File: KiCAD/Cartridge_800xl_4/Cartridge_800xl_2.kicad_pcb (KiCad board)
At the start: 4 copper layers, 64 x 80.2 mm, 21 parts, among them SW1 Reset, U1 27C512, U2 74HC165, U3 74HC595, U4 GAL16V8, U5 TXS0108EPW, U6 mini_esp32

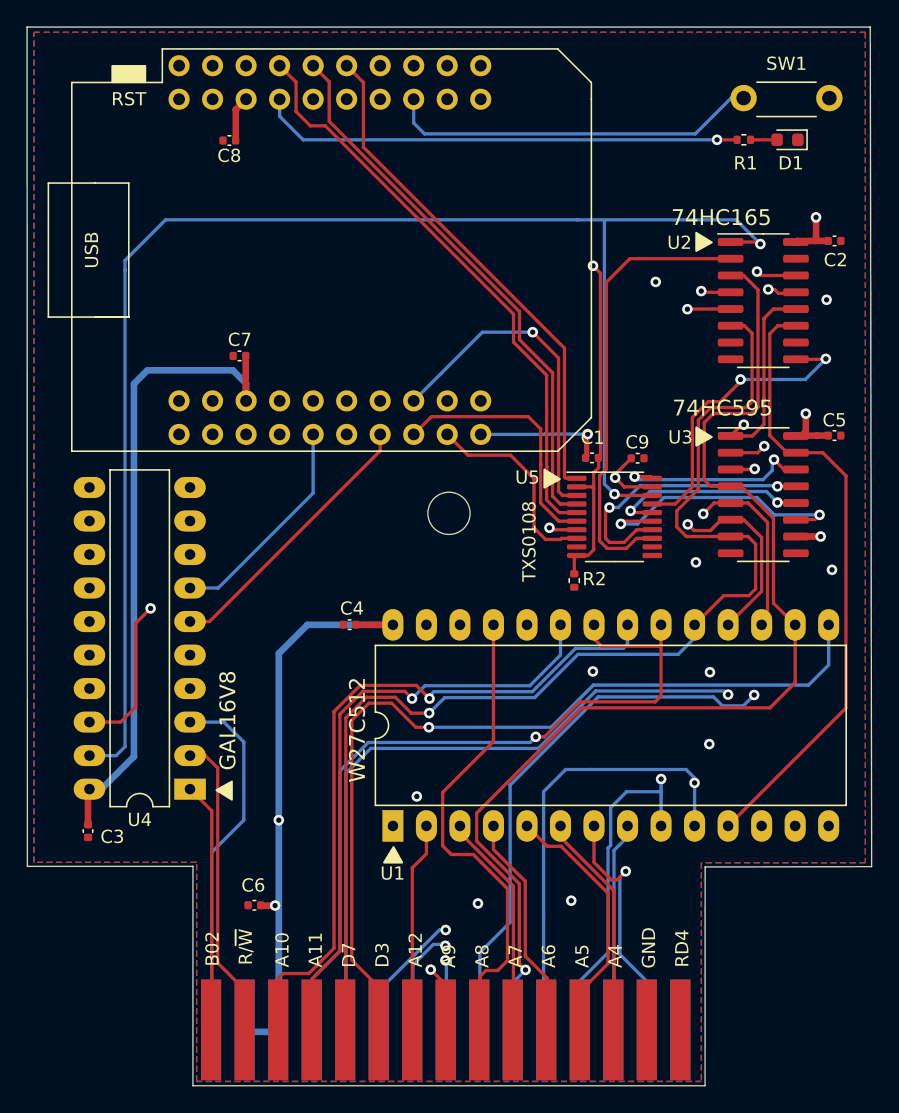
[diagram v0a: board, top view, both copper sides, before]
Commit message: version 3
No more sub version in file name
Fixed the userlist issue
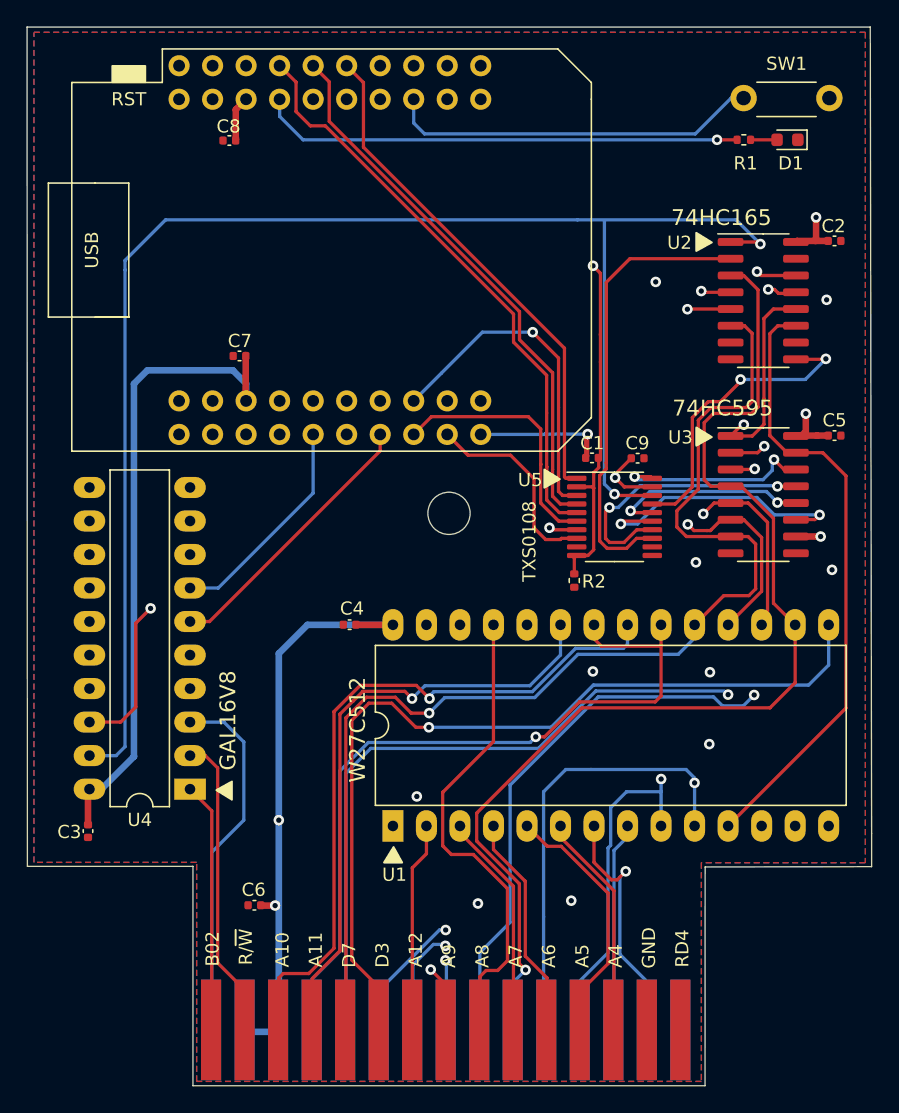
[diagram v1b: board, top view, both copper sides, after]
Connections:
- net IO1 renamed IO1H
- net IO2 renamed IO2H
- net iIO2 renamed IO2L
- U6 pad 25: iIO1 -> IO1L

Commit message: 3.78 release
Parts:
- moved C6 6.45 mm to (137.2, 120.3)
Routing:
- net +5V: track 201.9 -> 201.6 mm, vias 6 -> 5
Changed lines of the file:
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@@
   )
   (footprint "Capacitor_SMD:C_0402_1005Metric" (layer "F.Cu")
-    (at 136.900148 126.7125 180)
+    (at 137.2235 120.269 180)
     (descr "Capacitor SMD 0402 (1005 Metric), square (rectangular) end terminal, IPC_7351 nominal, (Body size source: IPC-SM-782 page 76, https://www.pcb-3d.com/wordpress/wp-content/uploads/ipc-sm-782a_amendment_1_and_2.pdf), generated with kicad-footprint-generator")
     (tags "capacitor")
@@
   (segment (start 136.240148 85.0125) (end 136.240148 86.6175) (width 0.5) (layer "F.Cu") (net 24))
   (segment (start 144.605148 105.461359) (end 144.595148 105.451359) (width 0.5) (layer "F.Cu") (net 24))
-  (segment (start 137.405148 126.7375) (end 137.380148 126.7125) (width 0.5) (layer "F.Cu") (net 24))
   (segment (start 136.240148 86.6175) (end 136.240148 88.4625) (width 0.5) (layer "F.Cu") (net 24))
   (segment (start 136.240148 88.4625) (end 136.270148 88.4925) (width 0.5) (layer "F.Cu") (net 24))
@@
   (segment (start 180.38048 76.37) (end 179.39798 76.37) (width 0.5) (layer "F.Cu") (net 24))
   (segment (start 179.46048 74.5825) (end 179.46048 76.3075) (width 0.5) (layer "F.Cu") (net 24))
+  (segment (start 138.743648 120.269) (end 138.747648 120.265) (width 0.5) (layer "F.Cu") (net 24))
+  (segment (start 137.7035 120.269) (end 138.743648 120.269) (width 0.5) (layer "F.Cu") (net 24))
   (segment (start 124.29 118.022648) (end 124.400148 117.9125) (width 0.5) (layer "F.Cu") (net 24))
   (segment (start 178.68548 89.4575) (end 178.68548 90.8075) (width 0.5) (layer "F.Cu") (net 24))
   (segment (start 164.9332 95.007) (end 164.2364 94.3102) (width 0.25) (layer "F.Cu") (net 24))
-  (segment (start 138.470148 126.7375) (end 137.405148 126.7375) (width 0.5) (layer "F.Cu") (net 24))
   (segment (start 147.395148 105.461359) (end 144.605148 105.461359) (width 0.5) (layer "F.Cu") (net 24))
   (segment (start 179.53548 91.12) (end 177.96548 91.12) (width 0.5) (layer "F.Cu") (net 24))
@@
   (via (at 164.2364 94.3102) (size 0.8) (drill 0.4) (layers "F.Cu" "B.Cu") (net 24))
   (via (at 138.747648 120.265) (size 0.8) (drill 0.4) (layers "F.Cu" "B.Cu") (net 24))
-  (via (at 138.470148 126.7375) (size 0.8) (drill 0.4) (layers "F.Cu" "B.Cu") (net 24))
   (via (at 178.68548 89.4575) (size 0.8) (drill 0.4) (layers "F.Cu" "B.Cu") (net 24))
   (segment (start 178.6636 99.822) (end 179.7156 98.77) (width 0.5) (layer "In1.Cu") (net 24))
@@
   (segment (start 127.769668 87.19798) (end 128.795148 86.1725) (width 0.5) (layer "B.Cu") (net 24))
   (segment (start 127.775148 115.4375) (end 127.769668 115.43202) (width 0.5) (layer "B.Cu") (net 24))
-  (segment (start 138.747648 126.735) (end 138.472648 126.735) (width 0.5) (layer "B.Cu") (net 24))
   (segment (start 138.747648 120.265) (end 138.747648 107.632352) (width 0.5) (layer "B.Cu") (net 24))
   (segment (start 140.918641 105.461359) (end 138.747648 107.632352) (width 0.5) (layer "B.Cu") (net 24))
@@
   (segment (start 135.265148 86.1725) (end 136.270148 87.1775) (width 0.5) (layer "B.Cu") (net 24))
   (segment (start 124.400148 117.9125) (end 125.300148 117.9125) (width 0.5) (layer "B.Cu") (net 24))
-  (segment (start 138.472648 126.735) (end 138.470148 126.7375) (width 0.5) (layer "B.Cu") (net 24))
   (segment (start 163.1188 85.5218) (end 163.1188 83.4644) (width 0.25) (layer "F.Cu") (net 26))
   (segment (start 135.485148 68.7375) (end 135.485148 66.4175) (width 0.5) (layer "F.Cu") (net 26))
